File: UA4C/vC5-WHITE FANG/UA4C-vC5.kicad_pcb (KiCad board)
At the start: 2 copper layers, 100 x 99.8 mm, 388 parts, among them IC2 IXDN602SIA, IC3 IXDN602SIA, J1 External MAP Conn, P1 INPUTS, P10 Dual VR C, P2 OUTPUTS, P3 SER0, P4 SER3, P5 SER2, P6 SPI0, P7 SPI1, P9 CAN, Q1 NCV8406, Q10 NCV8402AD, Q11 NCV8402AD, Q12 NCV8402AD, Q2 NCV8406, Q3 NCV8406, Q4 NCV8406, Q5 NCV8406, Q6 NCV8406, Q7 NCV8406, Q8 NCV8406, Q9 NCV8402AD, U1 KP234XTMA1, U2 2940-5.0, U3 MAP, U4 MP6600, U5 SN74LVC1G04DBV

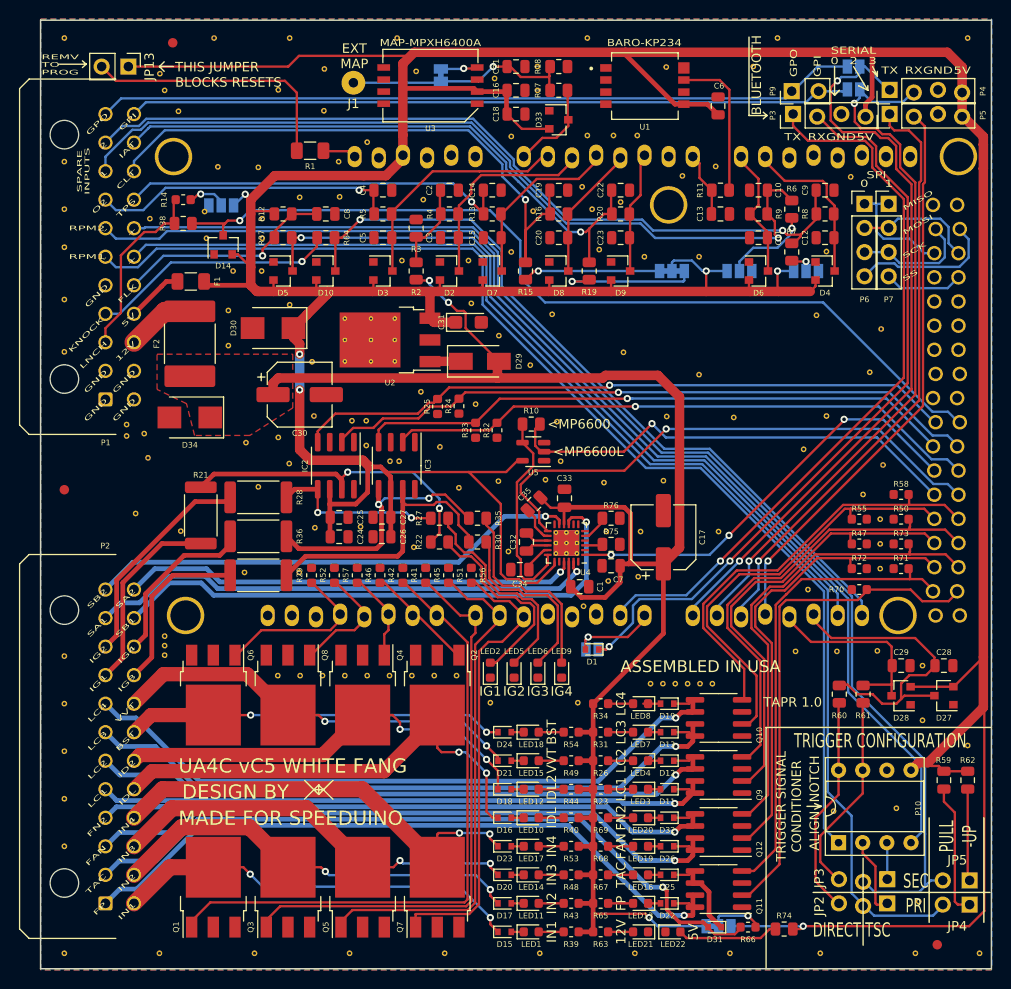
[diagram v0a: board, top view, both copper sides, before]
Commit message: Added TUNETECH logo instead of ASSEMBLED IN THE US
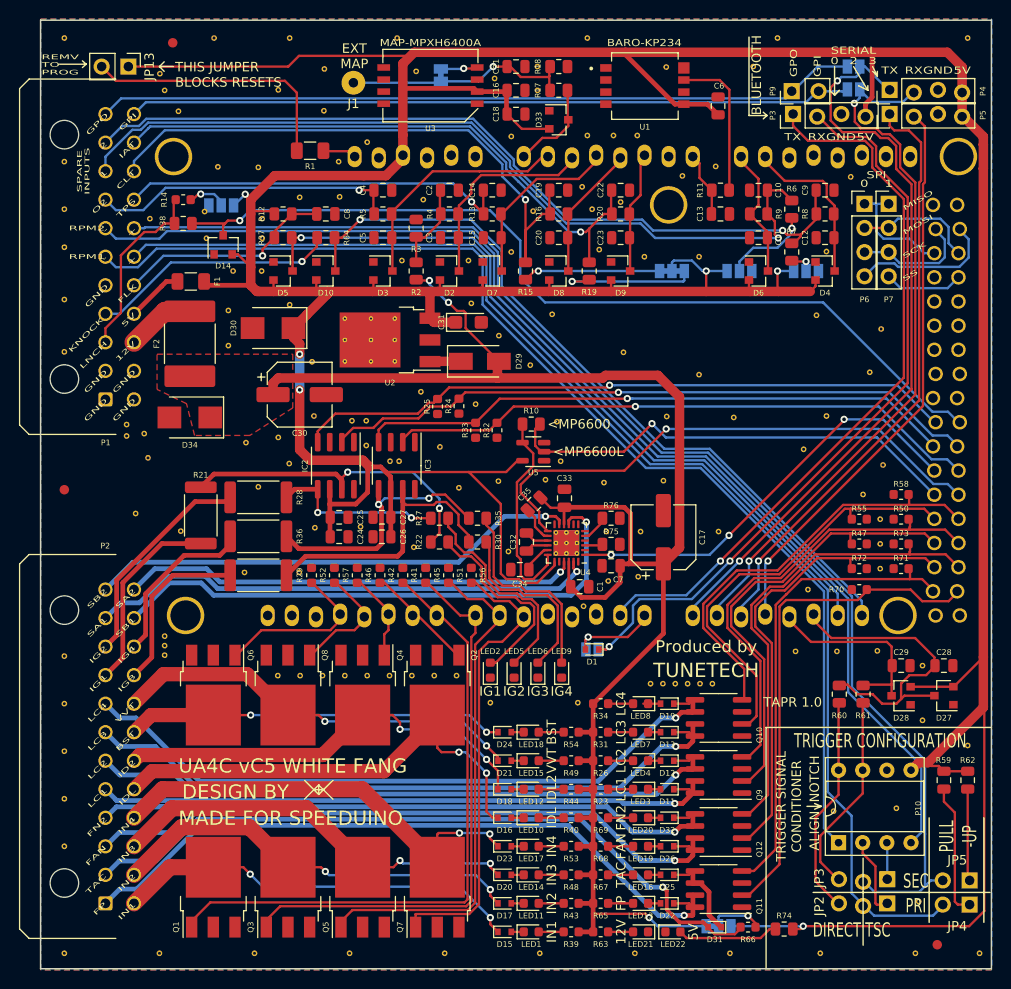
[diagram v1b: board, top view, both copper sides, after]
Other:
- board text added: "Produced by"
- board text added: "TUNETECH"
- board text removed: "ASSEMBLED IN USA"
